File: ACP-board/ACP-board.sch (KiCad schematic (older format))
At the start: 1 part

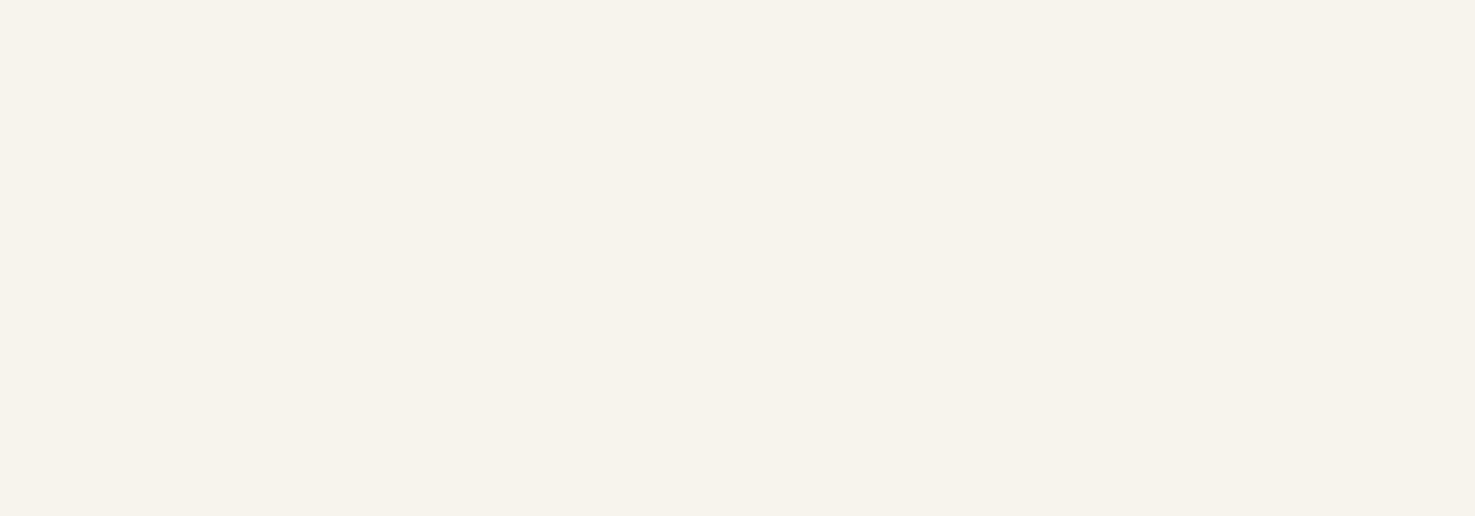
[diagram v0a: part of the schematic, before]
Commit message: Added basic input output circuits
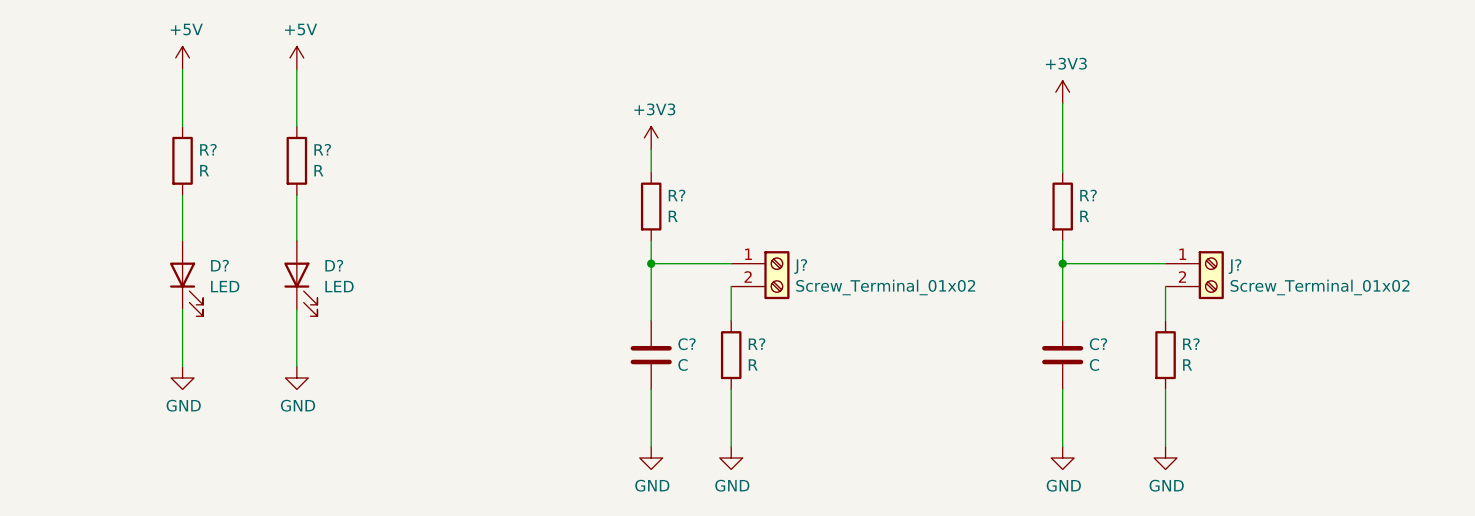
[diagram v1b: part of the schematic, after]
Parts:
- added C? (x2): C, symbol Device:C
- added D? (x2): LED, symbol Device:LED
- added J? (x2): Screw_Terminal_01x02, symbol Connector:Screw_Terminal_01x02
- added R? (x6): R, symbol Device:R
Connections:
- new net: D?.2 (A), R?.2 (x2)
- new net: C?.1, J?.1 (Pin_1), R?.2 (x2)
- new net: J?.2 (Pin_2), R?.1 (x2)
- new net +3V3: R?.1, R?.1
- new net +5V: R?.1, R?.1
- new net GND: C?.2, C?.2, D?.1 (K), D?.1 (K), R?.2, R?.2

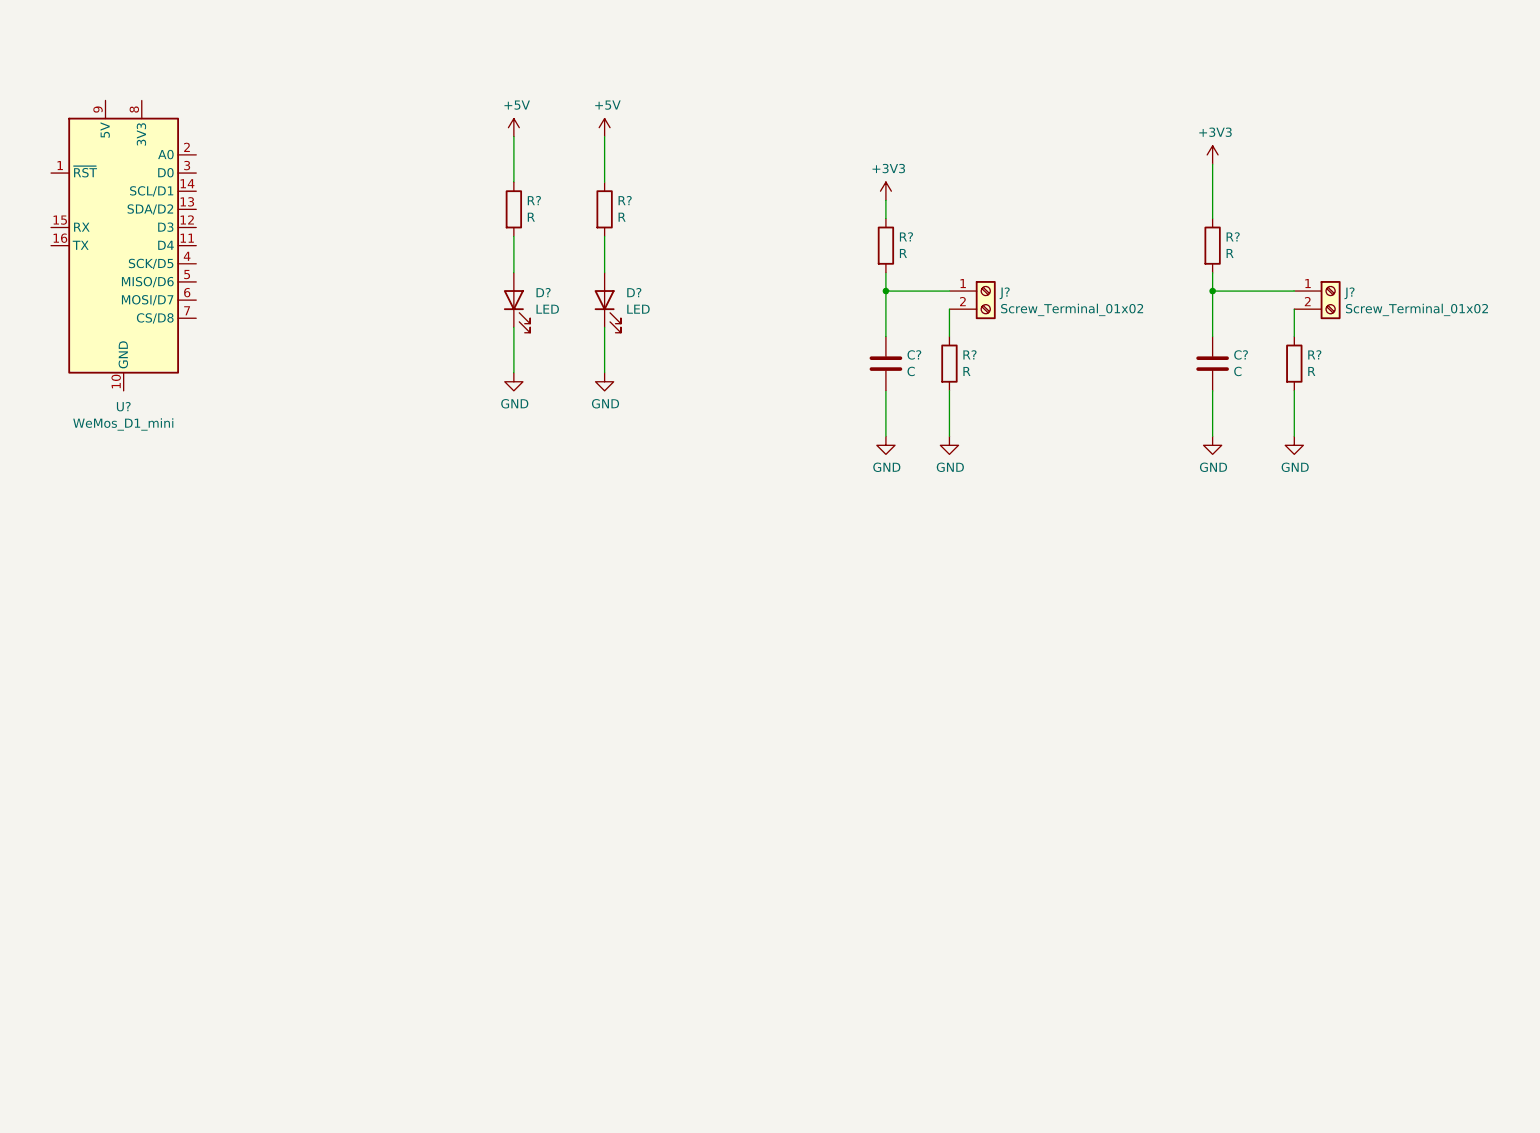
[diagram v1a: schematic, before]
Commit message: Added library for IRLML2502, updated schematic
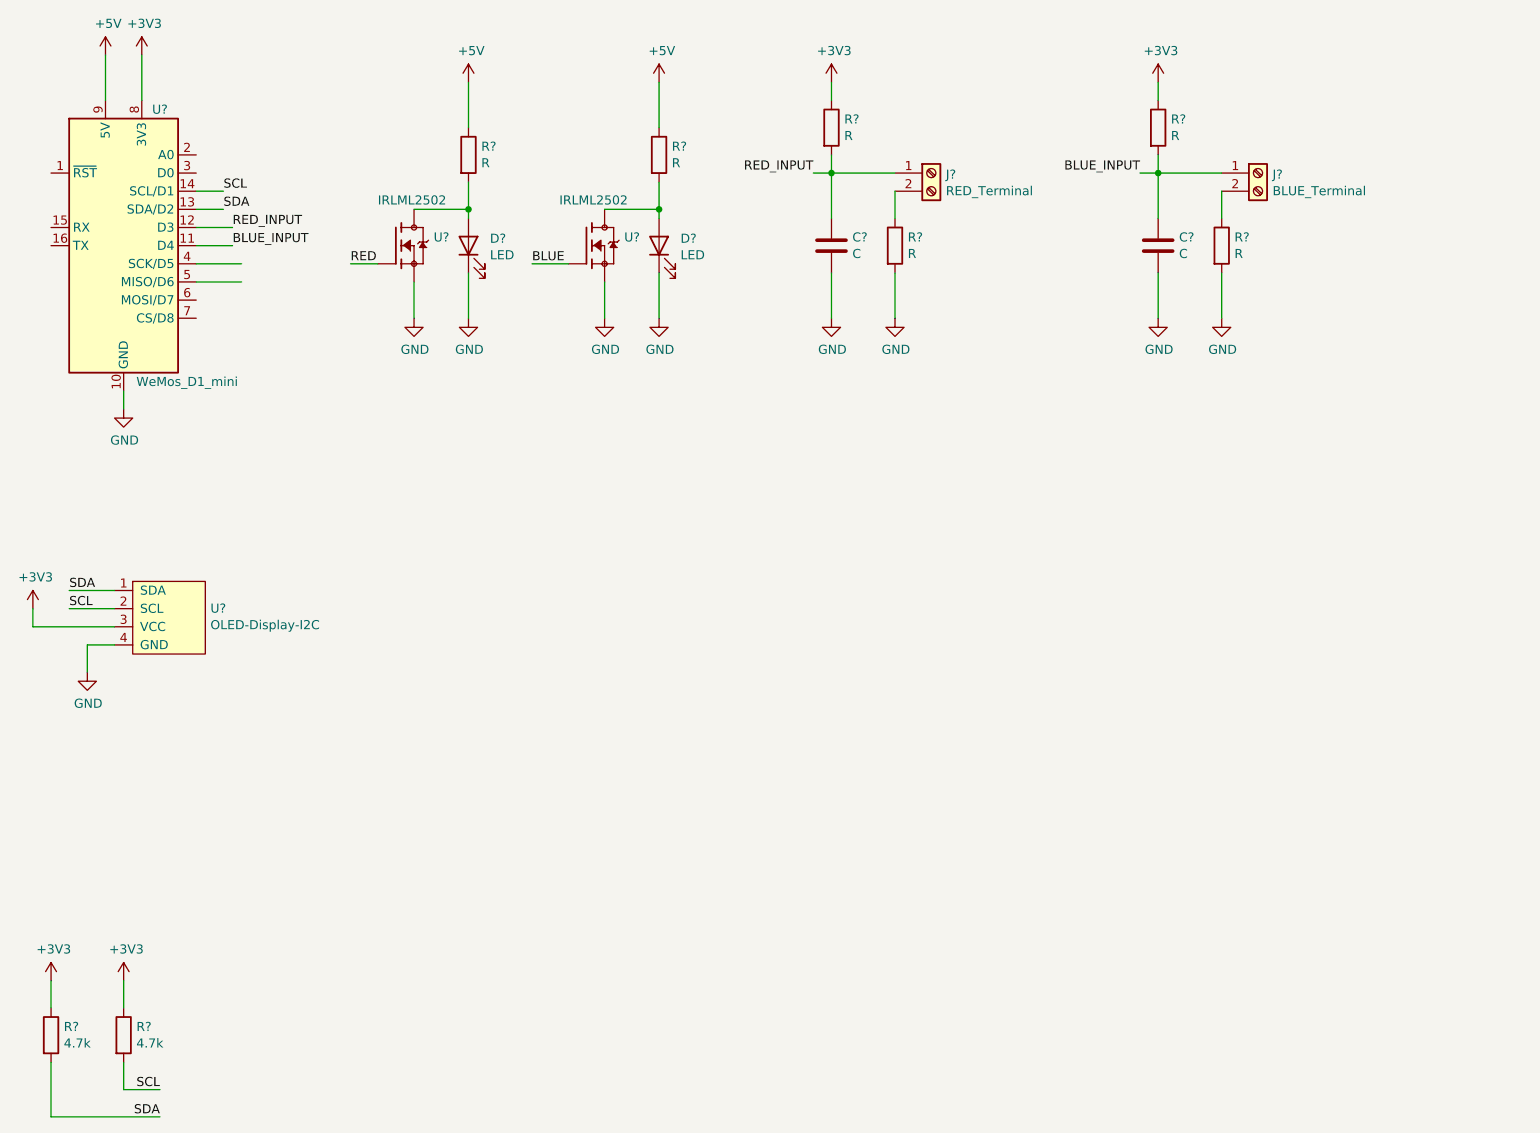
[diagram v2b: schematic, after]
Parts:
- added R? (x2): 4.7k, symbol Device:R
- added U?: OLED-Display-I2C, symbol OLED_Display:OLED-Display-I2C
- added U? (x2): IRLML2502, SOT23, symbol IRLML2502:IRLML2502
- J?: value Screw_Terminal_01x02 -> RED_Terminal
- J?: value Screw_Terminal_01x02 -> BLUE_Terminal
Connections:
- net labels added: BLUE, BLUE_INPUT, RED, RED_INPUT, SCL, SDA
- wire segments 20 -> 51
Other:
- moved on the sheet: C?, D?, J?, R?
